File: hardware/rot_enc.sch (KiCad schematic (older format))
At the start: 8 parts, among them J2 ROT_ENC_HEADER, SW14 ROT1

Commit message: update,
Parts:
- renumbered C22 to C39, C23 to C40, C24 to C41, J2 to J7, R17 to R28, R18 to R29, R19 to R30, SW14 to SW18
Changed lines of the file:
@@
 $EndDescr
 $Comp
-L taobao-components:EC11_VERTICAL SW14
+L taobao-components:EC11_VERTICAL SW18
 U 1 1 5D0A34E5
 P 3900 2700
-AR Path="/5CF34744/5D0A34E5" Ref="SW14"  Part="1"
+AR Path="/5CF34744/5D0A34E5" Ref="SW18"  Part="1"
 AR Path="/5CFF7883/5D0A34E5" Ref="SW?"  Part="1"
-F 0 "SW14" H 3900 2300 50  0000 C CNN
+F 0 "SW18" H 3900 2300 50  0000 C CNN
 F 1 "ROT1" H 3900 2400 50  0000 C CNN
 F 2 "footprint-lib:RotaryEncoder_Alps_EC11E_Vertical_H20mm" H 3900 2350 50  0001 C CNN
@@
 $EndBitmap
 $Comp
-L taobao-r:R273,0603 R17
+L taobao-r:R273,0603 R28
 U 1 1 5CED60AF
 P 3150 2300
-AR Path="/5CF34744/5CED60AF" Ref="R17"  Part="1"
+AR Path="/5CF34744/5CED60AF" Ref="R28"  Part="1"
 AR Path="/5CFF7883/5CED60AF" Ref="R?"  Part="1"
-F 0 "R17" V 2900 2300 50  0000 C CNN
+F 0 "R28" V 2900 2300 50  0000 C CNN
 F 1 "R273,0603" V 3000 2300 50  0000 C CNN
 F 2 "Resistor_SMD:R_0603_1608Metric_Pad1.05x0.95mm_HandSolder" H 3150 2300 50  0001 C CNN
@@
 $EndComp
 $Comp
-L taobao-r:R273,0603 R18
+L taobao-r:R273,0603 R29
 U 1 1 5D32A3BC
 P 3150 2800
-AR Path="/5CF34744/5D32A3BC" Ref="R18"  Part="1"
+AR Path="/5CF34744/5D32A3BC" Ref="R29"  Part="1"
 AR Path="/5CFF7883/5D32A3BC" Ref="R?"  Part="1"
-F 0 "R18" V 2900 2800 50  0000 C CNN
+F 0 "R29" V 2900 2800 50  0000 C CNN
 F 1 "R273,0603" V 3000 2800 50  0000 C CNN
 F 2 "Resistor_SMD:R_0603_1608Metric_Pad1.05x0.95mm_HandSolder" H 3150 2800 50  0001 C CNN
@@
 $EndComp
 $Comp
-L taobao-r:R273,0603 R19
+L taobao-r:R273,0603 R30
 U 1 1 5D32A3BD
 P 3150 3250
-AR Path="/5CF34744/5D32A3BD" Ref="R19"  Part="1"
+AR Path="/5CF34744/5D32A3BD" Ref="R30"  Part="1"
 AR Path="/5CFF7883/5D32A3BD" Ref="R?"  Part="1"
-F 0 "R19" V 2900 3250 50  0000 C CNN
+F 0 "R30" V 2900 3250 50  0000 C CNN
 F 1 "R273,0603" V 3000 3250 50  0000 C CNN
 F 2 "Resistor_SMD:R_0603_1608Metric_Pad1.05x0.95mm_HandSolder" H 3150 3250 50  0001 C CNN
@@
 $EndComp
 $Comp
-L taobao-c:C104,0603 C24
+L taobao-c:C104,0603 C41
 U 1 1 5D32A3BE
 P 2800 3450
-AR Path="/5CF34744/5D32A3BE" Ref="C24"  Part="1"
+AR Path="/5CF34744/5D32A3BE" Ref="C41"  Part="1"
 AR Path="/5CFF7883/5D32A3BE" Ref="C?"  Part="1"
-F 0 "C24" H 2900 3500 50  0000 L CNN
+F 0 "C41" H 2900 3500 50  0000 L CNN
 F 1 "C104,0603" H 2900 3450 50  0000 L CNN
 F 2 "Capacitor_SMD:C_0603_1608Metric_Pad1.05x0.95mm_HandSolder" H 2800 3450 50  0001 C CNN
@@
 $EndComp
 $Comp
-L taobao-c:C104,0603 C23
+L taobao-c:C104,0603 C40
 U 1 1 5D32A3BF
 P 2800 2950
-AR Path="/5CF34744/5D32A3BF" Ref="C23"  Part="1"
+AR Path="/5CF34744/5D32A3BF" Ref="C40"  Part="1"
 AR Path="/5CFF7883/5D32A3BF" Ref="C?"  Part="1"
-F 0 "C23" H 2900 3000 50  0000 L CNN
+F 0 "C40" H 2900 3000 50  0000 L CNN
 F 1 "C104,0603" H 2900 2950 50  0000 L CNN
 F 2 "Capacitor_SMD:C_0603_1608Metric_Pad1.05x0.95mm_HandSolder" H 2800 2950 50  0001 C CNN
@@
 $EndComp
 $Comp
-L taobao-c:C104,0603 C22
+L taobao-c:C104,0603 C39
 U 1 1 5CED75A5
 P 2800 2500
-AR Path="/5CF34744/5CED75A5" Ref="C22"  Part="1"
+AR Path="/5CF34744/5CED75A5" Ref="C39"  Part="1"
 AR Path="/5CFF7883/5CED75A5" Ref="C?"  Part="1"
-F 0 "C22" H 2900 2550 50  0000 L CNN
+F 0 "C39" H 2900 2550 50  0000 L CNN
 F 1 "C104,0603" H 2900 2500 50  0000 L CNN
 F 2 "Capacitor_SMD:C_0603_1608Metric_Pad1.05x0.95mm_HandSolder" H 2800 2500 50  0001 C CNN
@@
 	2800 3250 2800 3350
 $Comp
-L power:GND #PWR042
+L power:GND #PWR0149
 U 1 1 5CED86F3
 P 2800 2650
-AR Path="/5CF34744/5CED86F3" Ref="#PWR042"  Part="1"
+AR Path="/5CF34744/5CED86F3" Ref="#PWR0149"  Part="1"
 AR Path="/5CFF7883/5CED86F3" Ref="#PWR?"  Part="1"
-F 0 "#PWR042" H 2800 2400 50  0001 C CNN
+F 0 "#PWR0149" H 2800 2400 50  0001 C CNN
 F 1 "GND" H 2850 2450 50  0000 C CNN
 F 2 "" H 2800 2650 50  0001 C CNN
@@
 	2800 2650 2800 2600
 $Comp
-L power:GND #PWR044
+L power:GND #PWR0151
 U 1 1 5D32A3C2
 P 2800 3100
-AR Path="/5CF34744/5D32A3C2" Ref="#PWR044"  Part="1"
+AR Path="/5CF34744/5D32A3C2" Ref="#PWR0151"  Part="1"
 AR Path="/5CFF7883/5D32A3C2" Ref="#PWR?"  Part="1"
-F 0 "#PWR044" H 2800 2850 50  0001 C CNN
+F 0 "#PWR0151" H 2800 2850 50  0001 C CNN
 F 1 "GND" H 2850 2900 50  0000 C CNN
 F 2 "" H 2800 3100 50  0001 C CNN
@@
 	2800 3100 2800 3050
 $Comp
-L power:GND #PWR045
+L power:GND #PWR0152
 U 1 1 5CED8F95
 P 2800 3600
-AR Path="/5CF34744/5CED8F95" Ref="#PWR045"  Part="1"
+AR Path="/5CF34744/5CED8F95" Ref="#PWR0152"  Part="1"
 AR Path="/5CFF7883/5CED8F95" Ref="#PWR?"  Part="1"
-F 0 "#PWR045" H 2800 3350 50  0001 C CNN
+F 0 "#PWR0152" H 2800 3350 50  0001 C CNN
 F 1 "GND" H 2850 3400 50  0000 C CNN
 F 2 "" H 2800 3600 50  0001 C CNN
@@
 	2800 3600 2800 3550
 $Comp
-L power:GND #PWR041
+L power:GND #PWR0148
 U 1 1 5CED947F
 P 3350 2600
-AR Path="/5CF34744/5CED947F" Ref="#PWR041"  Part="1"
+AR Path="/5CF34744/5CED947F" Ref="#PWR0148"  Part="1"
 AR Path="/5CFF7883/5CED947F" Ref="#PWR?"  Part="1"
-F 0 "#PWR041" H 3350 2350 50  0001 C CNN
+F 0 "#PWR0148" H 3350 2350 50  0001 C CNN
 F 1 "GND" H 3400 2400 50  0000 C CNN
 F 2 "" H 3350 2600 50  0001 C CNN
@@
 $EndComp
 $Comp
-L power:GND #PWR043
+L power:GND #PWR0150
 U 1 1 5D32A3C5
 P 4400 2900
-AR Path="/5CF34744/5D32A3C5" Ref="#PWR043"  Part="1"
+AR Path="/5CF34744/5D32A3C5" Ref="#PWR0150"  Part="1"
 AR Path="/5CFF7883/5D32A3C5" Ref="#PWR?"  Part="1"
-F 0 "#PWR043" H 4400 2650 50  0001 C CNN
+F 0 "#PWR0150" H 4400 2650 50  0001 C CNN
 F 1 "GND" H 4450 2700 50  0000 C CNN
 F 2 "" H 4400 2900 50  0001 C CNN
@@
 ROT_ENC_A
 $Comp
-L Connector:Conn_01x03_Female J2
+L Connector:Conn_01x03_Female J7
 U 1 1 5CF225E9
 P 1100 2200
-AR Path="/5CF34744/5CF225E9" Ref="J2"  Part="1"
+AR Path="/5CF34744/5CF225E9" Ref="J7"  Part="1"
 AR Path="/5CFF7883/5CF225E9" Ref="J?"  Part="1"
-F 0 "J2" H 950 2500 50  0000 C CNN
+F 0 "J7" H 950 2500 50  0000 C CNN
 F 1 "ROT_ENC_HEADER" H 950 2400 50  0000 C CNN
 F 2 "Connector_PinHeader_1.27mm:PinHeader_1x03_P1.27mm_Vertical" H 1100 2200 50  0001 C CNN

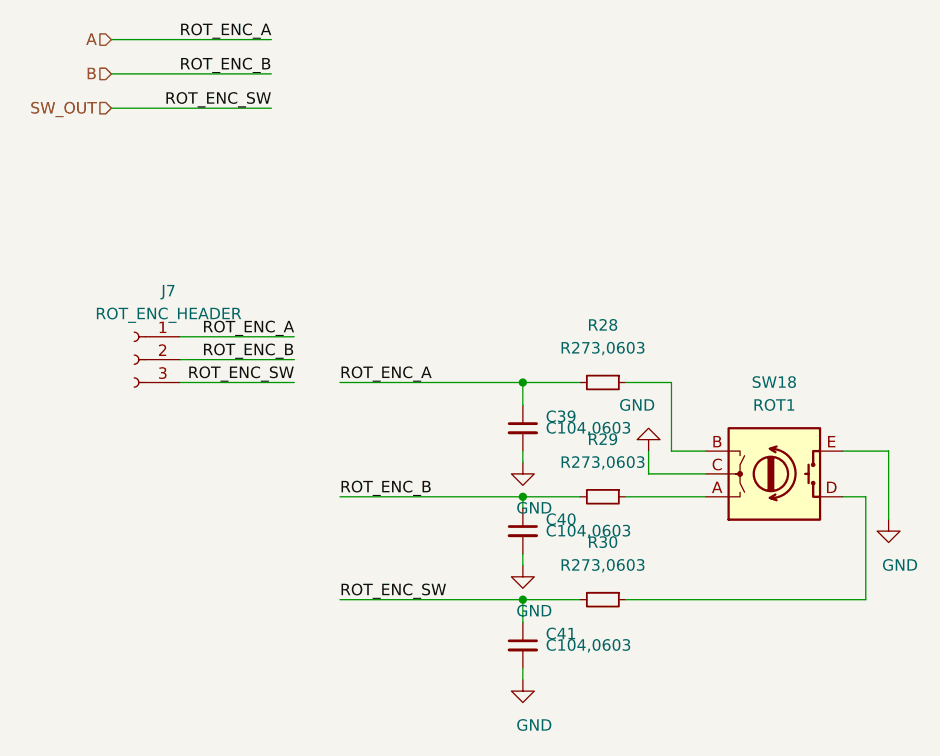
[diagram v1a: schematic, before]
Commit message: update for tidy tracks,
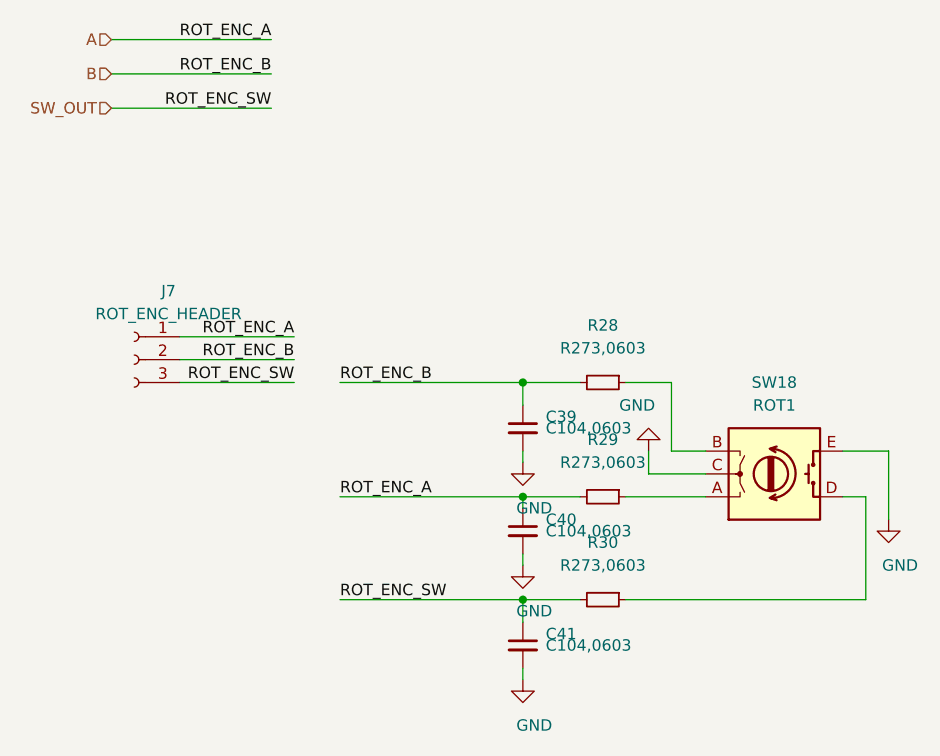
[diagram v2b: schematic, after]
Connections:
- net A: now also C40.1, R29.2; no longer C39.1, R28.2
- net B: now also C39.1, R28.2; no longer C40.1, R29.2
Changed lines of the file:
@@
 Wire Wire Line
 	4300 3250 3250 3250
+Text Label 2000 2800 0    50   ~ 0
+ROT_ENC_A
 Text Label 2000 2300 0    50   ~ 0
-ROT_ENC_A
-Text Label 2000 2800 0    50   ~ 0
 ROT_ENC_B
 Text Label 2000 3250 0    50   ~ 0
